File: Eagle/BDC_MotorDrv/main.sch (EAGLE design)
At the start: 1 part, among them U1 ATTINY10-TSHR

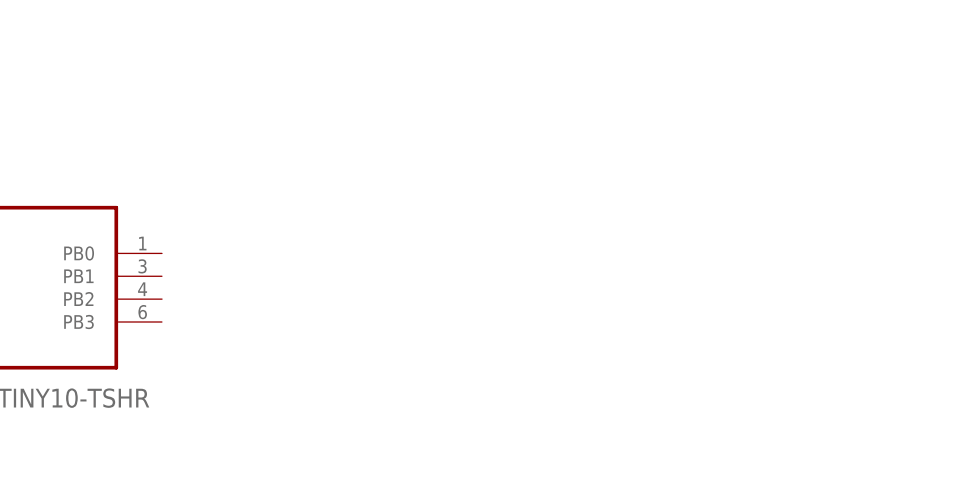
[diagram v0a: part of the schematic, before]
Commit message: Small cosmetic changes to schematic
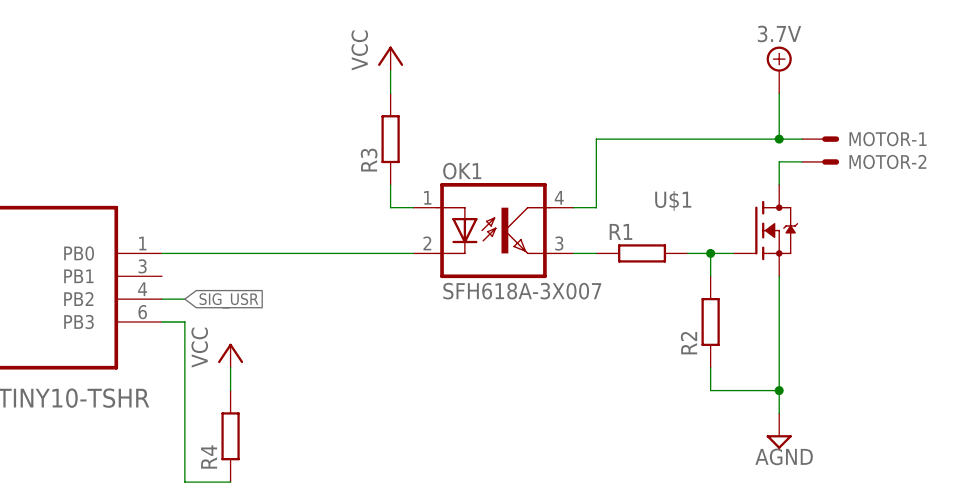
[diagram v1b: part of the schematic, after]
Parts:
- added MOTOR: 22-23-2021, con-molex:22-23-2021
- added OK1: SFH618A-3X007, optocoupler:SFH618A-3X007
- added R1, R2, R3, R4: (no value), rcl:R-EU_R0603
- added U$1: (no value), transistor-fet:IRLML0030
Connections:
- new net +12V: MOTOR-1.S, OK1.COL
- new net AGND: R2.1, U$1.S
- new net N$1: OK1.A, R3.1
- new net N$2: OK1.C, U1.PB0
- new net N$3: R1.2, R2.2, U$1.G
- new net N$4: MOTOR-2.S, U$1.D
- new net N$5: OK1.EMIT, R1.1
- new net N$6: R4.1, U1.PB3
- new net SIG_USR: U1.PB2
- net VCC: now also R3.2, R4.2
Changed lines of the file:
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@@
 <part name="P+1" library="supply1" deviceset="VCC" device=""/>
 <part name="GND1" library="supply1" deviceset="GND" device=""/>
+<part name="U$1" library="transistor-fet" deviceset="IRLML0030" device=""/>
+<part name="R1" library="rcl" deviceset="R-EU_" device="R0603"/>
+<part name="R2" library="rcl" deviceset="R-EU_" device="R0603"/>
+<part name="OK1" library="optocoupler" deviceset="SFH618?*" device="A-3X007"/>
+<part name="P+2" library="supply1" deviceset="VCC" device=""/>
+<part name="R3" library="rcl" deviceset="R-EU_" device="R0603"/>
+<part name="MOTOR_PWR" library="supply2" deviceset="+12V" device="" value="3.7V"/>
+<part name="MOTOR" library="con-molex" deviceset="22-23-2021" device="" value=""/>
+<part name="R4" library="rcl" deviceset="R-EU_" device="R0603"/>
+<part name="P+3" library="supply1" deviceset="VCC" device=""/>
+<part name="SUPPLY1" library="supply2" deviceset="AGND" device=""/>
 </parts>
 <sheets>
@@
 <instance part="P+1" gate="VCC" x="25.4" y="53.34"/>
 <instance part="GND1" gate="1" x="25.4" y="17.78"/>
+<instance part="U$1" gate="G$1" x="132.08" y="40.64"/>
+<instance part="R1" gate="G$1" x="119.38" y="38.1"/>
+<instance part="R2" gate="G$1" x="127" y="30.48" rot="R90"/>
+<instance part="OK1" gate="G$1" x="104.14" y="40.64"/>
+<instance part="P+2" gate="VCC" x="91.44" y="60.96"/>
+<instance part="R3" gate="G$1" x="91.44" y="50.8" rot="R90"/>
+<instance part="MOTOR_PWR" gate="+12V" x="134.62" y="58.42"/>
+<instance part="MOTOR" gate="-1" x="139.7" y="50.8"/>
+<instance part="MOTOR" gate="-2" x="139.7" y="48.26"/>
+<instance part="R4" gate="G$1" x="73.66" y="17.78" rot="R90"/>
+<instance part="P+3" gate="VCC" x="73.66" y="27.94"/>
+<instance part="SUPPLY1" gate="G$1" x="134.62" y="17.78"/>
 </instances>
 <busses>
@@
 <wire x1="25.4" y1="38.1" x2="25.4" y2="50.8" width="0.1524" layer="91"/>
 </segment>
+<segment>
+<pinref part="P+2" gate="VCC" pin="VCC"/>
+<pinref part="R3" gate="G$1" pin="2"/>
+<wire x1="91.44" y1="58.42" x2="91.44" y2="55.88" width="0.1524" layer="91"/>
+</segment>
+<segment>
+<pinref part="R4" gate="G$1" pin="2"/>
+<pinref part="P+3" gate="VCC" pin="VCC"/>
+<wire x1="73.66" y1="22.86" x2="73.66" y2="25.4" width="0.1524" layer="91"/>
+</segment>
 </net>
 <net name="GND" class="0">
@@
 </segment>
 </net>
+<net name="N$1" class="0">
+<segment>
+<pinref part="R3" gate="G$1" pin="1"/>
+<pinref part="OK1" gate="G$1" pin="A"/>
+<wire x1="91.44" y1="45.72" x2="91.44" y2="43.18" width="0.1524" layer="91"/>
+<wire x1="91.44" y1="43.18" x2="93.98" y2="43.18" width="0.1524" layer="91"/>
+</segment>
+</net>
+<net name="N$2" class="0">
+<segment>
+<pinref part="OK1" gate="G$1" pin="C"/>
+<pinref part="U1" gate="A" pin="PB0"/>
+<wire x1="93.98" y1="38.1" x2="66.04" y2="38.1" width="0.1524" layer="91"/>
+</segment>
+</net>
+<net name="N$3" class="0">
+<segment>
+<pinref part="R1" gate="G$1" pin="2"/>
+<pinref part="U$1" gate="G$1" pin="G"/>
+<wire x1="124.46" y1="38.1" x2="127" y2="38.1" width="0.1524" layer="91"/>
+<pinref part="R2" gate="G$1" pin="2"/>
+<wire x1="127" y1="38.1" x2="129.54" y2="38.1" width="0.1524" layer="91"/>
+<wire x1="127" y1="35.56" x2="127" y2="38.1" width="0.1524" layer="91"/>
+<junction x="127" y="38.1"/>
+</segment>
+</net>
+<net name="N$4" class="0">
+<segment>
+<pinref part="MOTOR" gate="-2" pin="S"/>
+<pinref part="U$1" gate="G$1" pin="D"/>
+<wire x1="137.16" y1="48.26" x2="134.62" y2="48.26" width="0.1524" layer="91"/>
+<wire x1="134.62" y1="48.26" x2="134.62" y2="45.72" width="0.1524" layer="91"/>
+</segment>
+</net>
+<net name="+12V" class="0">
+<segment>
+<pinref part="MOTOR" gate="-1" pin="S"/>
+<pinref part="MOTOR_PWR" gate="+12V" pin="+12V"/>
+<wire x1="137.16" y1="50.8" x2="134.62" y2="50.8" width="0.1524" layer="91"/>
+<wire x1="134.62" y1="50.8" x2="134.62" y2="55.88" width="0.1524" layer="91"/>
+<pinref part="OK1" gate="G$1" pin="COL"/>
+<wire x1="111.76" y1="43.18" x2="114.3" y2="43.18" width="0.1524" layer="91"/>
+<wire x1="114.3" y1="43.18" x2="114.3" y2="50.8" width="0.1524" layer="91"/>
+<wire x1="134.62" y1="50.8" x2="114.3" y2="50.8" width="0.1524" layer="91"/>
+<junction x="134.62" y="50.8"/>
+</segment>
+</net>
+<net name="N$5" class="0">
+<segment>
+<pinref part="OK1" gate="G$1" pin="EMIT"/>
+<pinref part="R1" gate="G$1" pin="1"/>
+<wire x1="111.76" y1="38.1" x2="114.3" y2="38.1" width="0.1524" layer="91"/>
+</segment>
+</net>
+<net name="N$6" class="0">
+<segment>
+<pinref part="U1" gate="A" pin="PB3"/>
+<pinref part="R4" gate="G$1" pin="1"/>
+<wire x1="66.04" y1="30.48" x2="68.58" y2="30.48" width="0.1524" layer="91"/>
+<wire x1="68.58" y1="30.48" x2="68.58" y2="12.7" width="0.1524" layer="91"/>
+<wire x1="68.58" y1="12.7" x2="73.66" y2="12.7" width="0.1524" layer="91"/>
+</segment>
+</net>
+<net name="SIG_USR" class="0">
+<segment>
+<pinref part="U1" gate="A" pin="PB2"/>
+<wire x1="66.04" y1="33.02" x2="68.58" y2="33.02" width="0.1524" layer="91"/>
+<label x="68.58" y="33.02" size="1.27" layer="95" xref="yes"/>
+</segment>
+</net>
+<net name="AGND" class="0">
+<segment>
+<pinref part="U$1" gate="G$1" pin="S"/>
+<wire x1="134.62" y1="35.56" x2="134.62" y2="22.86" width="0.1524" layer="91"/>
+<pinref part="R2" gate="G$1" pin="1"/>
+<wire x1="134.62" y1="22.86" x2="134.62" y2="20.32" width="0.1524" layer="91"/>
+<wire x1="127" y1="25.4" x2="127" y2="22.86" width="0.1524" layer="91"/>
+<wire x1="127" y1="22.86" x2="134.62" y2="22.86" width="0.1524" layer="91"/>
+<junction x="134.62" y="22.86"/>
+<pinref part="SUPPLY1" gate="G$1" pin="AGND"/>
+</segment>
+</net>

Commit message: First version of schematic finished
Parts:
- removed MOTOR: 22-23-2021, con-molex:22-23-2021
- added C1, C3, C4, C5: (no value), rcl:C-EUC0603K
- added C2: (no value), rcl:C-EUC1206K
- added D1, D2: (no value), diode:DIODE-MINIMELF
- added D3: (no value), diode:SUPPRESSOR-SMBJ
- added L1: (no value), rcl:L-EUL2012C
- added LED1: (no value), led:LEDSML0603
- added OK2: LTV816S, optocoupler:LTV816S
- added PAD1, PAD10, PAD2, PAD3, PAD6, PAD7, PAD8, PAD9: WIREPADSMD1,27-254, wirepad:WIREPADSMD1,27-254
- added PAD4, PAD5: WIREPADSMD2,54-5,08, wirepad:WIREPADSMD2,54-5,08
- added R5, R6, R7: (no value), rcl:R-EU_R0603
- added U$2: ASE, crystal:ASE
- OK1: value SFH618A-3X007 -> LTV816GEN; device optocoupler:SFH618A-3X007 -> optocoupler:LTV816GEN
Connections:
- removed net N$6: R4.1, U1.PB3
- removed net SIG_USR: U1.PB2
- new net #RESET: PAD6.P, R4.1, U$2.TRI, U1.PB3
- new net CLK/FEEDBACK: OK1.COL, PAD8.P, R7.1, U$2.OUT, U1.PB1
- new net INPUT_PWM: R5.1, U1.PB2
- new net MOTOR_PWM: OK2.C, PAD7.P, U1.PB0
- new net N$10: LED1.C, R2.2
- new net N$13: PAD3.P, R5.2
- new net N$7: OK2.EMIT, R1.2, U$1.G
- net +12V: now also C1.2, D1.C, OK2.COL, PAD4.P, PAD9.P; no longer MOTOR-1.S, OK1.COL
- net AGND: now also PAD5.P, R1.1; no longer R2.1
- net GND: now also C2.2, C3.2, C4.2, C5.2, D3.A, OK1.C, OK1.EMIT, PAD2.P, R2.1, U$2.GND
- net N$1: now also OK2.A; no longer OK1.A
- net N$2: now also OK1.A, R6.1; no longer OK1.C, U1.PB0
- net N$3: now also D2.A, D3.C, PAD1.P; no longer R1.2, R2.2, U$1.G
- net N$4: now also C1.1, D1.A, PAD10.P; no longer MOTOR-2.S
- net N$5: now also C4.1, D2.C, L1.1; no longer OK1.EMIT, R1.1
- net VCC: now also C2.1, C3.1, C5.1, L1.2, LED1.A, R6.2, R7.2, U$2.VDD
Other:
- note added: "CONFIG 1"
- note added: "CONFIG 2"
- note added: "MOTOR DRIVER"
- moved on the sheet: OK1, R1, R2, R3, R4, U$1, U1

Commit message: Initial board setup
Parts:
- renumbered PAD1 to VIN, PAD2 to VGND, PAD3 to PWM, PAD4 to M_VIN, PAD5 to M_GND
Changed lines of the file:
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@@
 <part name="P+4" library="supply1" deviceset="VCC" device=""/>
 <part name="GND2" library="supply1" deviceset="GND" device=""/>
-<part name="PAD1" library="wirepad" deviceset="WIREPAD" device="SMD1,27-254"/>
-<part name="PAD2" library="wirepad" deviceset="WIREPAD" device="SMD1,27-254"/>
-<part name="PAD3" library="wirepad" deviceset="WIREPAD" device="SMD1,27-254"/>
-<part name="PAD4" library="wirepad" deviceset="WIREPAD" device="SMD2,54-5,08"/>
-<part name="PAD5" library="wirepad" deviceset="WIREPAD" device="SMD2,54-5,08"/>
+<part name="VIN" library="wirepad" deviceset="WIREPAD" device="SMD1,27-254"/>
+<part name="VGND" library="wirepad" deviceset="WIREPAD" device="SMD1,27-254"/>
+<part name="PWM" library="wirepad" deviceset="WIREPAD" device="SMD1,27-254"/>
+<part name="M_VIN" library="wirepad" deviceset="WIREPAD" device="SMD2,54-5,08"/>
+<part name="M_GND" library="wirepad" deviceset="WIREPAD" device="SMD2,54-5,08"/>
 <part name="P+5" library="supply1" deviceset="VCC" device=""/>
 <part name="GND3" library="supply1" deviceset="GND" device=""/>
@@
 <instance part="P+4" gate="VCC" x="7.62" y="96.52"/>
 <instance part="GND2" gate="1" x="7.62" y="73.66"/>
-<instance part="PAD1" gate="G$1" x="-30.48" y="91.44"/>
-<instance part="PAD2" gate="G$1" x="-30.48" y="78.74"/>
-<instance part="PAD3" gate="G$1" x="-30.48" y="66.04"/>
-<instance part="PAD4" gate="G$1" x="-30.48" y="48.26"/>
-<instance part="PAD5" gate="G$1" x="-30.48" y="40.64"/>
+<instance part="VIN" gate="G$1" x="-30.48" y="91.44"/>
+<instance part="VGND" gate="G$1" x="-30.48" y="78.74"/>
+<instance part="PWM" gate="G$1" x="-30.48" y="66.04"/>
+<instance part="M_VIN" gate="G$1" x="-30.48" y="48.26"/>
+<instance part="M_GND" gate="G$1" x="-30.48" y="40.64"/>
 <instance part="P+5" gate="VCC" x="15.24" y="15.24"/>
 <instance part="GND3" gate="1" x="15.24" y="-15.24"/>
@@
 </segment>
 <segment>
-<pinref part="PAD5" gate="G$1" pin="P"/>
+<pinref part="M_GND" gate="G$1" pin="P"/>
 <pinref part="SUPPLY2" gate="G$1" pin="AGND"/>
 <wire x1="-27.94" y1="40.64" x2="-22.86" y2="40.64" width="0.1524" layer="91"/>
@@
 </segment>
 <segment>
-<pinref part="PAD4" gate="G$1" pin="P"/>
+<pinref part="M_VIN" gate="G$1" pin="P"/>
 <pinref part="MOTOR_PWR1" gate="+12V" pin="+12V"/>
 <wire x1="-27.94" y1="48.26" x2="-22.86" y2="48.26" width="0.1524" layer="91"/>
@@
 <wire x1="-20.32" y1="88.9" x2="-20.32" y2="91.44" width="0.1524" layer="91"/>
 <junction x="-20.32" y="91.44"/>
-<pinref part="PAD1" gate="G$1" pin="P"/>
+<pinref part="VIN" gate="G$1" pin="P"/>
 </segment>
 </net>
@@
 <pinref part="GND2" gate="1" pin="GND"/>
 <wire x1="7.62" y1="78.74" x2="7.62" y2="76.2" width="0.1524" layer="91"/>
-<pinref part="PAD2" gate="G$1" pin="P"/>
+<pinref part="VGND" gate="G$1" pin="P"/>
 </segment>
 <segment>
@@
 <segment>
 <pinref part="R5" gate="G$1" pin="2"/>
-<pinref part="PAD3" gate="G$1" pin="P"/>
+<pinref part="PWM" gate="G$1" pin="P"/>
 <wire x1="-25.4" y1="66.04" x2="-27.94" y2="66.04" width="0.1524" layer="91"/>
 </segment>

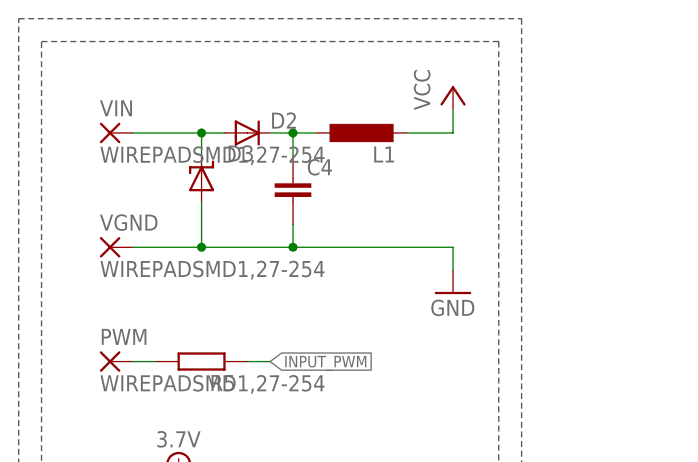
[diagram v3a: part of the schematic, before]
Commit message: Removed redundant power filtering
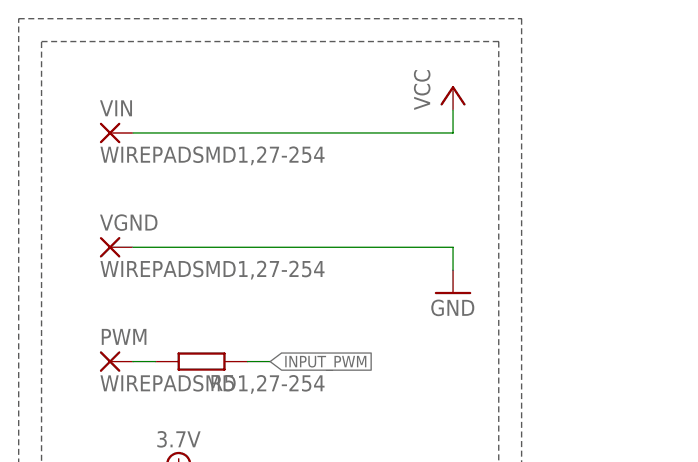
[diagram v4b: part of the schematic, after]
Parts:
- removed C4: (no value), rcl:C-EUC0603K
- removed D2: (no value), diode:DIODE-MINIMELF
- removed D3: (no value), diode:SUPPRESSOR-SMBJ
- removed L1: (no value), rcl:L-EUL2012C
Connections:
- removed net N$3: D2.A, D3.C, VIN.P
- removed net N$5: C4.1, D2.C, L1.1
- net GND: no longer C4.2, D3.A
- net VCC: now also VIN.P; no longer L1.2
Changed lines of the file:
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@@
 <part name="D1" library="diode" deviceset="DIODE-" device="MINIMELF"/>
 <part name="C1" library="rcl" deviceset="C-EU" device="C0603K"/>
-<part name="D2" library="diode" deviceset="DIODE-" device="MINIMELF"/>
 <part name="C2" library="rcl" deviceset="C-EU" device="C1206K"/>
 <part name="C3" library="rcl" deviceset="C-EU" device="C0603K"/>
@@
 <part name="FRAME1" library="frames" deviceset="A4L-LOC" device=""/>
 <part name="R2" library="rcl" deviceset="R-EU_" device="R0603"/>
-<part name="D3" library="diode" deviceset="SUPPRESSOR-" device="SMBJ"/>
-<part name="C4" library="rcl" deviceset="C-EU" device="C0603K"/>
-<part name="L1" library="rcl" deviceset="L-EU" device="L2012C"/>
 <part name="P+4" library="supply1" deviceset="VCC" device=""/>
 <part name="GND2" library="supply1" deviceset="GND" device=""/>
@@
 <instance part="D1" gate="G$1" x="175.26" y="7.62" rot="R90"/>
 <instance part="C1" gate="G$1" x="170.18" y="5.08" rot="R180"/>
-<instance part="D2" gate="G$1" x="-15.24" y="91.44"/>
 <instance part="C2" gate="G$1" x="33.02" y="-2.54"/>
 <instance part="C3" gate="G$1" x="25.4" y="-2.54"/>
@@
 <instance part="FRAME1" gate="G$1" x="-48.26" y="-68.58"/>
 <instance part="R2" gate="G$1" x="15.24" y="-5.08" rot="R90"/>
-<instance part="D3" gate="G$1" x="-20.32" y="86.36"/>
-<instance part="C4" gate="G$1" x="-10.16" y="86.36"/>
-<instance part="L1" gate="G$1" x="-2.54" y="91.44" rot="R90"/>
 <instance part="P+4" gate="VCC" x="7.62" y="96.52"/>
 <instance part="GND2" gate="1" x="7.62" y="73.66"/>
@@
 </segment>
 <segment>
-<pinref part="L1" gate="G$1" pin="2"/>
-<wire x1="2.54" y1="91.44" x2="7.62" y2="91.44" width="0.1524" layer="91"/>
 <pinref part="P+4" gate="VCC" pin="VCC"/>
 <wire x1="7.62" y1="93.98" x2="7.62" y2="91.44" width="0.1524" layer="91"/>
+<pinref part="VIN" gate="G$1" pin="P"/>
+<wire x1="7.62" y1="91.44" x2="-27.94" y2="91.44" width="0.1524" layer="91"/>
 </segment>
 <segment>
@@
 </segment>
 </net>
-<net name="N$3" class="0">
-<segment>
-<pinref part="D2" gate="G$1" pin="A"/>
-<wire x1="-17.78" y1="91.44" x2="-20.32" y2="91.44" width="0.1524" layer="91"/>
-<pinref part="D3" gate="G$1" pin="C"/>
-<wire x1="-20.32" y1="91.44" x2="-27.94" y2="91.44" width="0.1524" layer="91"/>
-<wire x1="-20.32" y1="88.9" x2="-20.32" y2="91.44" width="0.1524" layer="91"/>
-<junction x="-20.32" y="91.44"/>
-<pinref part="VIN" gate="G$1" pin="P"/>
-</segment>
-</net>
-<net name="N$5" class="0">
-<segment>
-<pinref part="D2" gate="G$1" pin="C"/>
-<pinref part="L1" gate="G$1" pin="1"/>
-<wire x1="-12.7" y1="91.44" x2="-10.16" y2="91.44" width="0.1524" layer="91"/>
-<pinref part="C4" gate="G$1" pin="1"/>
-<wire x1="-10.16" y1="91.44" x2="-7.62" y2="91.44" width="0.1524" layer="91"/>
-<wire x1="-10.16" y1="88.9" x2="-10.16" y2="91.44" width="0.1524" layer="91"/>
-<junction x="-10.16" y="91.44"/>
-</segment>
-</net>
 <net name="GND" class="0">
 <segment>
-<pinref part="D3" gate="G$1" pin="A"/>
-<wire x1="-20.32" y1="83.82" x2="-20.32" y2="78.74" width="0.1524" layer="91"/>
-<wire x1="-20.32" y1="78.74" x2="-27.94" y2="78.74" width="0.1524" layer="91"/>
-<pinref part="C4" gate="G$1" pin="2"/>
-<wire x1="-20.32" y1="78.74" x2="-10.16" y2="78.74" width="0.1524" layer="91"/>
-<wire x1="-10.16" y1="78.74" x2="-10.16" y2="81.28" width="0.1524" layer="91"/>
-<junction x="-20.32" y="78.74"/>
-<wire x1="-10.16" y1="78.74" x2="7.62" y2="78.74" width="0.1524" layer="91"/>
-<junction x="-10.16" y="78.74"/>
+<wire x1="-27.94" y1="78.74" x2="7.62" y2="78.74" width="0.1524" layer="91"/>
 <pinref part="GND2" gate="1" pin="GND"/>
 <wire x1="7.62" y1="78.74" x2="7.62" y2="76.2" width="0.1524" layer="91"/>
